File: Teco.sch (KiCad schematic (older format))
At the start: 54 parts, among them Q1 BC848, Q2 BC807, Q3 IRLML9303, SW1 SWITCH_2x

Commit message: Sch updated Layout done
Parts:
- removed C2: 0.1u, Capacitors:CAP_0603, symbol C
- removed F1: Fuse0R, Resistors:RES_0603_FUSE, symbol Fuse0R
- removed HOLE1, HOLE2, HOLE3, HOLE4: HOLE_METALLED, PCB:Hole2d4_out4d5mm, symbol HOLE_METALLED
- removed Q2: BC807, SOT:SOT23-3, symbol PNP
- removed R3: 100k, Resistors:RES_0603, symbol R
- removed R8: DNM, Resistors:RES_0603, symbol R
- removed SW1: SWITCH_2x, BtnsSwitches:BTN_PSM6, symbol SWITCH_2x
- added C12: 0.1u, Capacitors:CAP_0603, symbol C
- added C13: 10n, Capacitors:CAP_0603, symbol C
- added D4: PMEG2020, Diodes:SOD323, symbol D_Shottky
- added L1, L2: BLM15AG102, Inductors:IND_0402, symbol L
- added Q2: BC848, SOT:SOT23-3, symbol NPN
- added R23: 1M, Resistors:RES_0603, symbol R
- added SW1: BUTTON, BtnsSwitches:BTN_4x4_SMD, symbol BUTTON
- D1: footprint (none) -> LEDs:LED_0603
- D2: footprint (none) -> LEDs:LED_0603; Color Red -> Green
- D3: footprint (none) -> LEDs:LED_0603; Color Green -> Blue
- DA1: footprint (none) -> SOT:SOT223
- Q3: Price 7.2 -> (none)
- R12: value 1k -> 10k
- R13: value 5R1 -> 10k
- R14: value 1k -> 100k
- XL1: footprint (none) -> Connectors:USBmicro_MOLEX_WM17142
- XL2: footprint (none) -> Connectors:PLS-4
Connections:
- net labels added: 5VIN, GNDIN
- wire segments 152 -> 141
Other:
- note removed: "5R1 => 120mA max"

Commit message: Sent to production
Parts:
- XL3: footprint Connectors:PBS-6R -> Connectors:PBS-6R-MIRR
- XL4: footprint Connectors:PBS-2R -> Connectors:PBS-2R-MIRR
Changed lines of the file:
@@
 Board ident:\nPC13=0
 $Comp
-L GND #PWR011
+L GND #PWR010
 U 1 1 5901EAD2
 P 3200 4250
-F 0 "#PWR011" H 3290 4230 30  0001 C CNN
+F 0 "#PWR010" H 3290 4230 30  0001 C CNN
 F 1 "GND" H 3200 4170 30  0001 C CNN
 F 2 "" H 3200 4250 60  0000 C CNN
@@
 $EndComp
 $Comp
-L GND #PWR012
+L GND #PWR011
 U 1 1 5901F28F
 P 5850 4000
-F 0 "#PWR012" H 5940 3980 30  0001 C CNN
+F 0 "#PWR011" H 5940 3980 30  0001 C CNN
 F 1 "GND" H 5850 3920 30  0001 C CNN
 F 2 "" H 5850 4000 60  0000 C CNN
@@
 $EndComp
 $Comp
-L GND #PWR013
+L GND #PWR012
 U 1 1 5901F3AF
 P 6100 4000
-F 0 "#PWR013" H 6190 3980 30  0001 C CNN
+F 0 "#PWR012" H 6190 3980 30  0001 C CNN
 F 1 "GND" H 6100 3920 30  0001 C CNN
 F 2 "" H 6100 4000 60  0000 C CNN
@@
 $EndComp
 $Comp
-L GND #PWR014
+L GND #PWR013
 U 1 1 5901F45F
 P 6350 4000
-F 0 "#PWR014" H 6440 3980 30  0001 C CNN
+F 0 "#PWR013" H 6440 3980 30  0001 C CNN
 F 1 "GND" H 6350 3920 30  0001 C CNN
 F 2 "" H 6350 4000 60  0000 C CNN
@@
 $EndComp
 $Comp
-L GND #PWR015
+L GND #PWR014
 U 1 1 59020374
 P 9750 550
-F 0 "#PWR015" H 9840 530 30  0001 C CNN
+F 0 "#PWR014" H 9840 530 30  0001 C CNN
 F 1 "GND" H 9750 470 30  0001 C CNN
 F 2 "" H 9750 550 60  0000 C CNN
@@
 F 0 "XL3" H 10578 1657 50  0000 L CNN
 F 1 "CONN_6" H 10578 1566 50  0000 L CNN
-F 2 "Connectors:PBS-6R" V 10300 1500 60  0001 C CNN
+F 2 "Connectors:PBS-6R-MIRR" V 10300 1500 60  0001 C CNN
 F 3 "" V 10400 1600 60  0001 C CNN
 F 4 "0" V 10600 1800 60  0001 C CNN "SolderPoints"
@@
 RXD
 $Comp
-L GND #PWR016
+L GND #PWR015
 U 1 1 59020D2A
 P 10150 1550
-F 0 "#PWR016" H 10240 1530 30  0001 C CNN
+F 0 "#PWR015" H 10240 1530 30  0001 C CNN
 F 1 "GND" H 10150 1470 30  0001 C CNN
 F 2 "" H 10150 1550 60  0000 C CNN
@@
 $EndComp
 $Comp
-L GND #PWR017
+L GND #PWR016
 U 1 1 59021F2D
 P 7450 6300
-F 0 "#PWR017" H 7540 6280 30  0001 C CNN
+F 0 "#PWR016" H 7540 6280 30  0001 C CNN
 F 1 "GND" H 7450 6220 30  0001 C CNN
 F 2 "" H 7450 6300 60  0000 C CNN
@@
 T_JRST
 $Comp
-L GND #PWR018
+L GND #PWR017
 U 1 1 5902498F
 P 2300 1600
-F 0 "#PWR018" H 2390 1580 30  0001 C CNN
+F 0 "#PWR017" H 2390 1580 30  0001 C CNN
 F 1 "GND" H 2300 1520 30  0001 C CNN
 F 2 "" H 2300 1600 60  0000 C CNN
@@
 $EndComp
 $Comp
-L GND #PWR019
+L GND #PWR018
 U 1 1 59027B26
 P 10000 5450
-F 0 "#PWR019" H 10090 5430 30  0001 C CNN
+F 0 "#PWR018" H 10090 5430 30  0001 C CNN
 F 1 "GND" H 10000 5370 30  0001 C CNN
 F 2 "" H 10000 5450 60  0000 C CNN
@@
 $EndComp
 $Comp
-L +3.3V #PWR020
+L +3.3V #PWR019
 U 1 1 59027C46
 P 10000 6050
-F 0 "#PWR020" H 10000 6010 30  0001 C CNN
+F 0 "#PWR019" H 10000 6010 30  0001 C CNN
 F 1 "+3.3V" H 10038 6118 30  0000 C CNN
 F 2 "" H 10000 6050 60  0000 C CNN
@@
 	1200 7450 1200 7400
 $Comp
-L GND #PWR021
+L GND #PWR020
 U 1 1 59028E7A
 P 2700 7200
-F 0 "#PWR021" H 2790 7180 30  0001 C CNN
+F 0 "#PWR020" H 2790 7180 30  0001 C CNN
 F 1 "GND" H 2700 7120 30  0001 C CNN
 F 2 "" H 2700 7200 60  0000 C CNN
@@
 $EndComp
 $Comp
-L +3.3V #PWR022
+L +3.3V #PWR021
 U 1 1 5902A6EC
 P 7650 1350
-F 0 "#PWR022" H 7650 1310 30  0001 C CNN
+F 0 "#PWR021" H 7650 1310 30  0001 C CNN
 F 1 "+3.3V" H 7689 1418 30  0000 C CNN
 F 2 "" H 7650 1350 60  0000 C CNN
@@
 	7650 1350 7800 1350
 $Comp
-L GND #PWR023
+L GND #PWR022
 U 1 1 5902A95C
 P 7700 1550
-F 0 "#PWR023" H 7790 1530 30  0001 C CNN
+F 0 "#PWR022" H 7790 1530 30  0001 C CNN
 F 1 "GND" H 7700 1470 30  0001 C CNN
 F 2 "" H 7700 1550 60  0000 C CNN
@@
 	4500 7250 4400 7250
 $Comp
-L +3.3V #PWR024
+L +3.3V #PWR023
 U 1 1 5902CE63
 P 4500 6650
-F 0 "#PWR024" H 4500 6610 30  0001 C CNN
+F 0 "#PWR023" H 4500 6610 30  0001 C CNN
 F 1 "+3.3V" V 4539 6687 30  0000 L CNN
 F 2 "" H 4500 6650 60  0000 C CNN
@@
 Connection ~ 4850 6950
 $Comp
-L GND #PWR025
+L GND #PWR024
 U 1 1 5902DE60
 P 4850 7600
-F 0 "#PWR025" H 4940 7580 30  0001 C CNN
+F 0 "#PWR024" H 4940 7580 30  0001 C CNN
 F 1 "GND" H 4850 7520 30  0001 C CNN
 F 2 "" H 4850 7600 60  0000 C CNN
@@
 $EndComp
 $Comp
-L GND #PWR026
+L GND #PWR025
 U 1 1 5902ED5A
 P 1250 1700
-F 0 "#PWR026" H 1340 1680 30  0001 C CNN
+F 0 "#PWR025" H 1340 1680 30  0001 C CNN
 F 1 "GND" H 1250 1620 30  0001 C CNN
 F 2 "" H 1250 1700 60  0000 C CNN
@@
 $EndComp
 $Comp
-L GND #PWR027
+L GND #PWR026
 U 1 1 59031CF8
 P 3800 5850
-F 0 "#PWR027" H 3890 5830 30  0001 C CNN
+F 0 "#PWR026" H 3890 5830 30  0001 C CNN
 F 1 "GND" H 3800 5770 30  0001 C CNN
 F 2 "" H 3800 5850 60  0000 C CNN
@@
 $EndComp
 $Comp
-L GND #PWR028
+L GND #PWR027
 U 1 1 59031D06
 P 4950 5850
-F 0 "#PWR028" H 5040 5830 30  0001 C CNN
+F 0 "#PWR027" H 5040 5830 30  0001 C CNN
 F 1 "GND" H 4950 5770 30  0001 C CNN
 F 2 "" H 4950 5850 60  0000 C CNN
@@
 	4950 5850 4950 5750
 $Comp
-L +5V #PWR029
+L +5V #PWR028
 U 1 1 590322EA
 P 2700 6700
-F 0 "#PWR029" H 2700 6660 30  0001 C CNN
+F 0 "#PWR028" H 2700 6660 30  0001 C CNN
 F 1 "+5V" H 2738 6768 30  0000 C CNN
 F 2 "" H 2700 6700 60  0000 C CNN
@@
 $EndComp
 $Comp
-L +5V #PWR030
+L +5V #PWR029
 U 1 1 590323CE
 P 4850 6250
-F 0 "#PWR030" H 4850 6210 30  0001 C CNN
+F 0 "#PWR029" H 4850 6210 30  0001 C CNN
 F 1 "+5V" V 4889 6288 30  0000 L CNN
 F 2 "" H 4850 6250 60  0000 C CNN
@@
 	4850 6250 4850 6350
 $Comp
-L +5V #PWR031
+L +5V #PWR030
 U 1 1 59032DF7
 P 3650 5250
-F 0 "#PWR031" H 3650 5210 30  0001 C CNN
+F 0 "#PWR030" H 3650 5210 30  0001 C CNN
 F 1 "+5V" H 3689 5318 30  0000 C CNN
 F 2 "" H 3650 5250 60  0000 C CNN
@@
 Connection ~ 4750 5250
 $Comp
-L GND #PWR032
+L GND #PWR031
 U 1 1 59033228
 P 4250 5850
-F 0 "#PWR032" H 4340 5830 30  0001 C CNN
+F 0 "#PWR031" H 4340 5830 30  0001 C CNN
 F 1 "GND" H 4250 5770 30  0001 C CNN
 F 2 "" H 4250 5850 60  0000 C CNN
@@
 	4250 5650 4250 5850
 $Comp
-L +3.3V #PWR033
+L +3.3V #PWR032
 U 1 1 59033A01
 P 5050 5250
-F 0 "#PWR033" H 5050 5210 30  0001 C CNN
+F 0 "#PWR032" H 5050 5210 30  0001 C CNN
 F 1 "+3.3V" H 5088 5318 30  0000 C CNN
 F 2 "" H 5050 5250 60  0000 C CNN
@@
 F 0 "XL4" H 10577 2328 40  0000 L CNN
 F 1 "CONN_2" H 10577 2252 40  0000 L CNN
-F 2 "Connectors:PBS-2R" H 10450 2300 60  0001 C CNN
+F 2 "Connectors:PBS-2R-MIRR" H 10450 2300 60  0001 C CNN
 F 3 "" H 10450 2300 60  0000 C CNN
 	1    10450 2300
@@
 $EndComp
 $Comp
-L GND #PWR034
+L GND #PWR033
 U 1 1 5902104A
 P 8000 2550
-F 0 "#PWR034" H 8090 2530 30  0001 C CNN
+F 0 "#PWR033" H 8090 2530 30  0001 C CNN
 F 1 "GND" H 8000 2470 30  0001 C CNN
 F 2 "" H 8000 2550 60  0000 C CNN
@@
 $EndComp
 $Comp
-L GND #PWR035
+L GND #PWR034
 U 1 1 59027180
 P 8000 4450
-F 0 "#PWR035" H 8090 4430 30  0001 C CNN
+F 0 "#PWR034" H 8090 4430 30  0001 C CNN
 F 1 "GND" H 8000 4370 30  0001 C CNN
 F 2 "" H 8000 4450 60  0000 C CNN
@@
 $EndComp
 $Comp
-L +3.3V #PWR036
+L +3.3V #PWR035
 U 1 1 59027B66
 P 7850 3200
-F 0 "#PWR036" H 7850 3160 30  0001 C CNN
+F 0 "#PWR035" H 7850 3160 30  0001 C CNN
 F 1 "+3.3V" H 7889 3268 30  0000 C CNN
 F 2 "" H 7850 3200 60  0000 C CNN
@@
 $EndComp
 $Comp
-L GND #PWR037
+L GND #PWR036
 U 1 1 59029D6C
 P 9850 4450
-F 0 "#PWR037" H 9940 4430 30  0001 C CNN
+F 0 "#PWR036" H 9940 4430 30  0001 C CNN
 F 1 "GND" H 9850 4370 30  0001 C CNN
 F 2 "" H 9850 4450 60  0000 C CNN

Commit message: + R to discharge pwr line
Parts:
- added R?: 10k, Resistors:RES_0603, symbol R
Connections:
- wire segments 141 -> 143
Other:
- note added: "Add it somehow\nWill not switch off\nwithout it"

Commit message: + v3 Sent to factory
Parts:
- removed C13: 10n, Capacitors:CAP_0603, symbol C
- removed L1, L2: BLM15AG102, Inductors:IND_0402, symbol L
- removed Q1: BC848, SOT:SOT23-3, symbol NPN
- removed R2, R5, R9: 10k, Resistors:RES_0603, symbol R
- removed R6: 36k, Resistors:RES_0603, symbol R
- removed R7: 100R, Resistors:RES_0603, symbol R
- removed XL1: USB_MINI_B, Connectors:USBmicro_MOLEX_WM17142, symbol USB_MINI_B
- added C2: 2u2, Capacitors:CAP_0603, symbol Tittar_kl:C
- added D5, D6, D7, D8: PESD3V3, Diodes:SOD323, symbol Tittar_kl:ZenerBidir
- added L1: 90R, Inductors:DLW21SN, symbol Tittar_kl:CHOKE_COIL
- added L2, L3: BLM18EG221SN1D, Inductors:IND_0603, symbol Tittar_kl:L
- added R2: 2R0, Resistors:RES_0603, symbol Tittar_kl:R
- added R5, R6: 22R, Resistors:RES_0603, symbol Tittar_kl:R
- added XL1: USB_MICRO_2H, Connectors:USBmicro_MOLEX_1050170001, symbol Connectors_kl:USB_MICRO_2H
- C1, C10, C11, C12, C3, C4, C5, C6, C7, C8, C9: symbol C -> Tittar_kl:C
- D1, D2, D3: symbol LED -> Tittar_kl:LED
- D4: symbol D_Shottky -> Tittar_kl:D_Shottky
- DA1: symbol LD1117 -> Power_kl:LD1117
- DD1: symbol STM32F10X-48 -> st_kl:STM32F10X-48
- HOLE5: symbol HOLE_METALLED -> pcb_details:HOLE_METALLED
- Logo1: symbol Logo -> pcb_details:Logo
- Q2: symbol NPN -> Transistors_kl:NPN
- Q3: symbol P_3PIN -> Transistors_kl:P_3PIN
- R1, R10, R11, R12, R13, R14, R15, R16, R18, R19, R20, R21, R23, R4: symbol R -> Tittar_kl:R
- R17, R22: value 4k7 -> 10k; symbol R -> Tittar_kl:R
- R3: renamed from R?; symbol R -> Tittar_kl:R
- SW1: symbol BUTTON -> Switches:BUTTON
- XL2: symbol CONN_4 -> Connectors_kl:CONN_4
- XL3: symbol CONN_6 -> Connectors_kl:CONN_6
- XL4: symbol CONN_2 -> Connectors_kl:CONN_2
- XTAL1: symbol CRYSTAL_H -> Tittar_kl:CRYSTAL_H
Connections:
- net labels added: +3v3, USB_DIN+, USB_DIN-
- net labels removed: +3.3V, USB_RENUM
- wire segments 143 -> 172
- no-connect marks 18 -> 23
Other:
- note added: "Will not switch off\nwithout it"
- note removed: "Add it somehow\nWill not switch off\nwithout it"
- note removed: "Board ident:\nPC13=0"

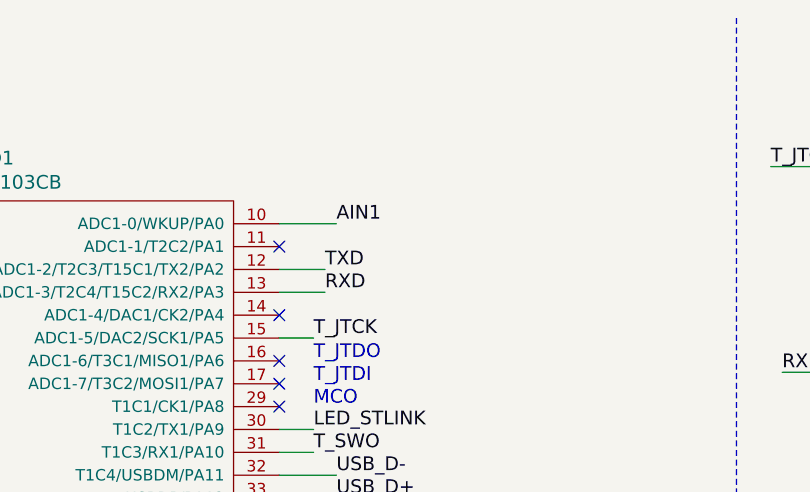
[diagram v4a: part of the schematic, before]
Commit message: v3.1: + Pull-up on RX + legend
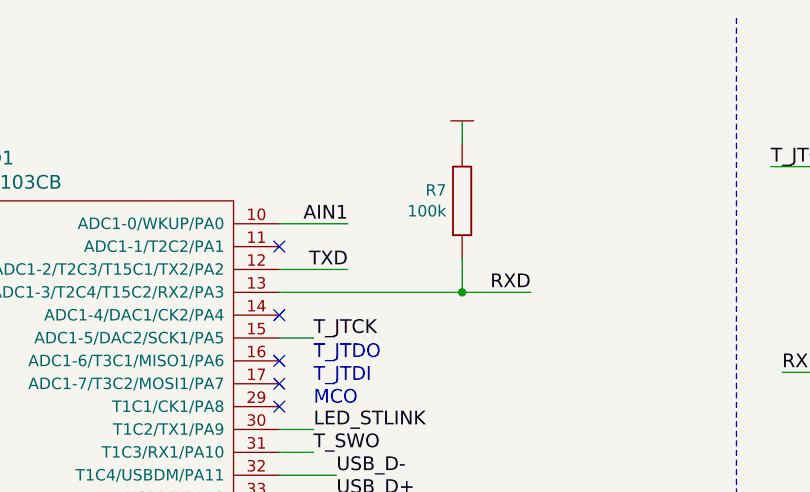
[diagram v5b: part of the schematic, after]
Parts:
- added R7: 100k, Resistors:RES_0603, symbol Tittar_kl:R
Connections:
- net GND: now also R7.2
- net RXD: now also R7.1
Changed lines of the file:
@@
-EESchema Schematic File Version 5
+EESchema Schematic File Version 4
 LIBS:Teco-cache
 EELAYER 29 0
@@
 	1    0    0    1
 $EndComp
-Text Label 5200 1400 0    60   ~ 0
+Text Label 5250 1400 2    60   ~ 0
 AIN1
 NoConn ~ 4950 1500
-Text Label 5150 1600 0    60   ~ 0
+Text Label 5250 1600 2    60   ~ 0
 TXD
-Text Label 5150 1700 0    60   ~ 0
+Text Label 6050 1700 2    60   ~ 0
 RXD
 $Comp
@@
 	9100 700  9100 800
 Wire Wire Line
-	4950 1400 5200 1400
-Wire Wire Line
-	5150 1700 4950 1700
-Wire Wire Line
-	4950 1600 5150 1600
-Wire Wire Line
 	10150 1700 10250 1700
 Wire Wire Line
@@
 Wire Wire Line
 	6000 7500 6150 7500
+$Comp
+L Tittar_kl:R R7
+U 1 1 5CBE8341
+P 5750 1300
+F 0 "R7" H 5681 1254 50  0000 R CNN
+F 1 "100k" H 5681 1345 50  0000 R CNN
+F 2 "Resistors:RES_0603" V 5830 1400 28  0001 C CNN
+F 3 "" V 5830 1150 60  0000 C CNN
+F 4 "0.5" V 5930 1250 60  0001 C CNN "Price"
+F 5 "2" V 6030 1350 60  0001 C CNN "SolderPoints"
+	1    5750 1300
+	1    0    0    1
+$EndComp
+$Comp
+L power:GND #PWR09
+U 1 1 5CBE834B
+P 5750 950
+F 0 "#PWR09" H 5840 930 30  0001 C CNN
+F 1 "GND" H 5750 870 30  0001 C CNN
+F 2 "" H 5750 950 60  0000 C CNN
+F 3 "" H 5750 950 60  0000 C CNN
+	1    5750 950
+	1    0    0    1
+$EndComp
+Wire Wire Line
+	5750 950  5750 1050
+Wire Wire Line
+	4950 1700 5750 1700
+Wire Wire Line
+	5750 1550 5750 1700
+Connection ~ 5750 1700
+Wire Wire Line
+	5750 1700 6050 1700
+Wire Wire Line
+	4950 1600 5250 1600
+Wire Wire Line
+	4950 1400 5250 1400
 $EndSCHEMATC
